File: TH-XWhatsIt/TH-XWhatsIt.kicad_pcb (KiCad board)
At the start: 2 copper layers, 175 x 128.1 mm, 36 parts, among them J1 MODEL F, J2 EXPANSION, J3 EXPANSION HEADER, J4 EXPANSION BEAMSPRING, J5 BEAMSPRING CONNECTOR, J6 EXPANSION BEAMSPRING, J7 EXPANSION DISPLAYWRITER, J8 DISPLAYWRITER CONNECTOR, J9 EXPANSION DISPLAYWRITER, SW1 SW_Push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

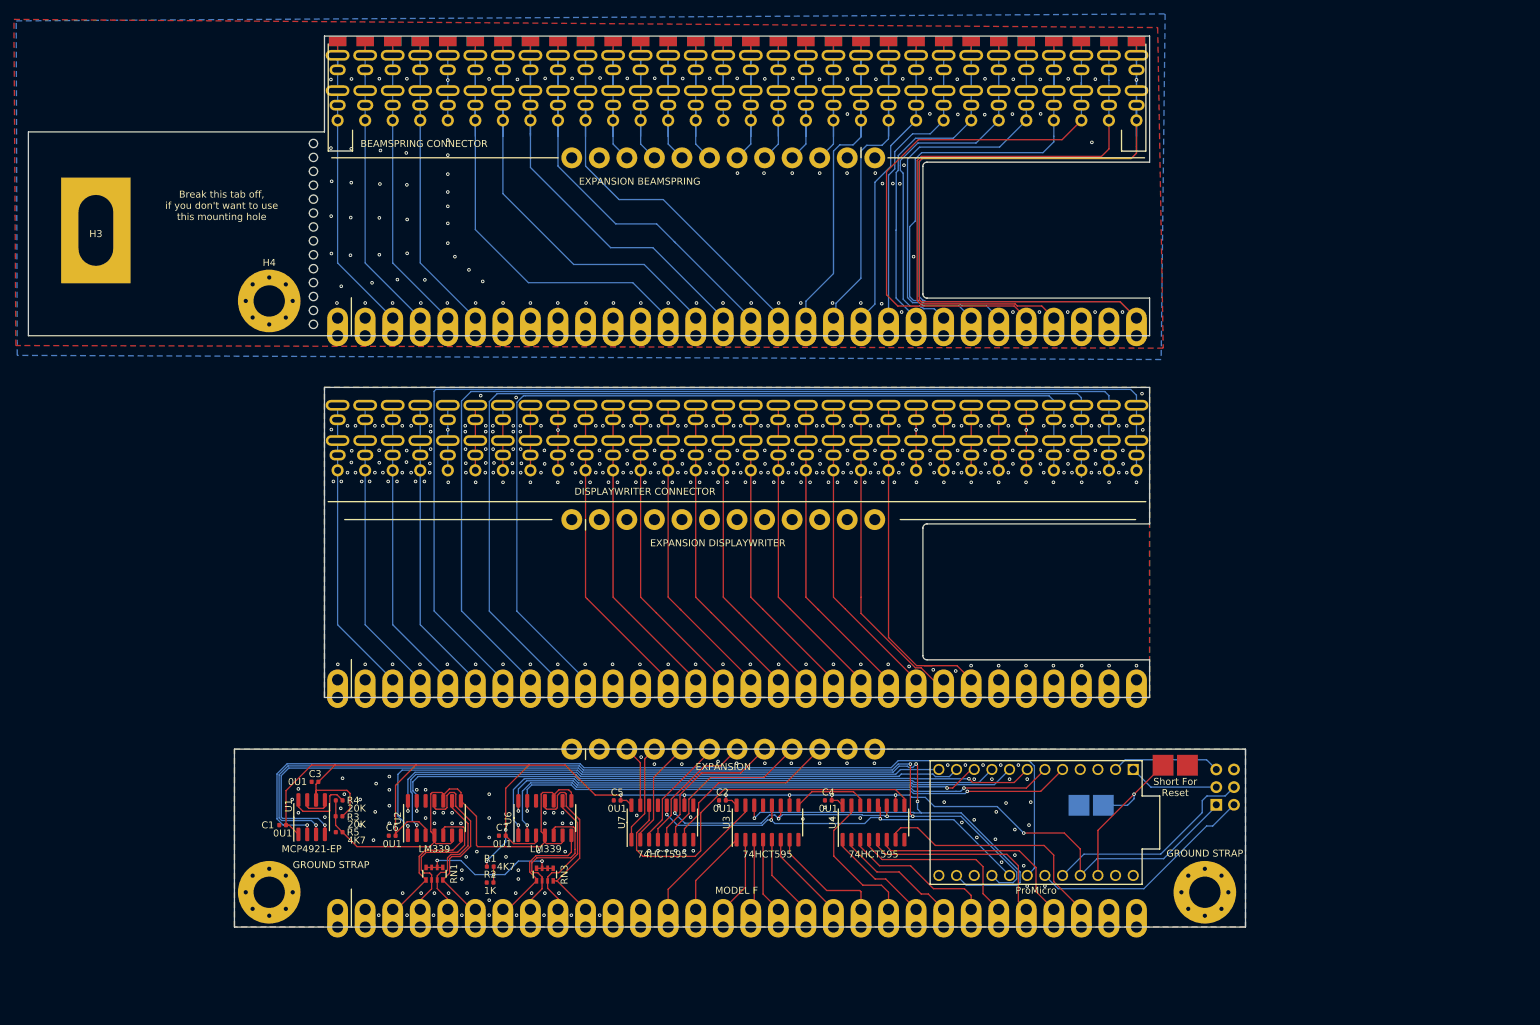
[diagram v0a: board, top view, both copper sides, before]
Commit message: Added compact beamspring-only version
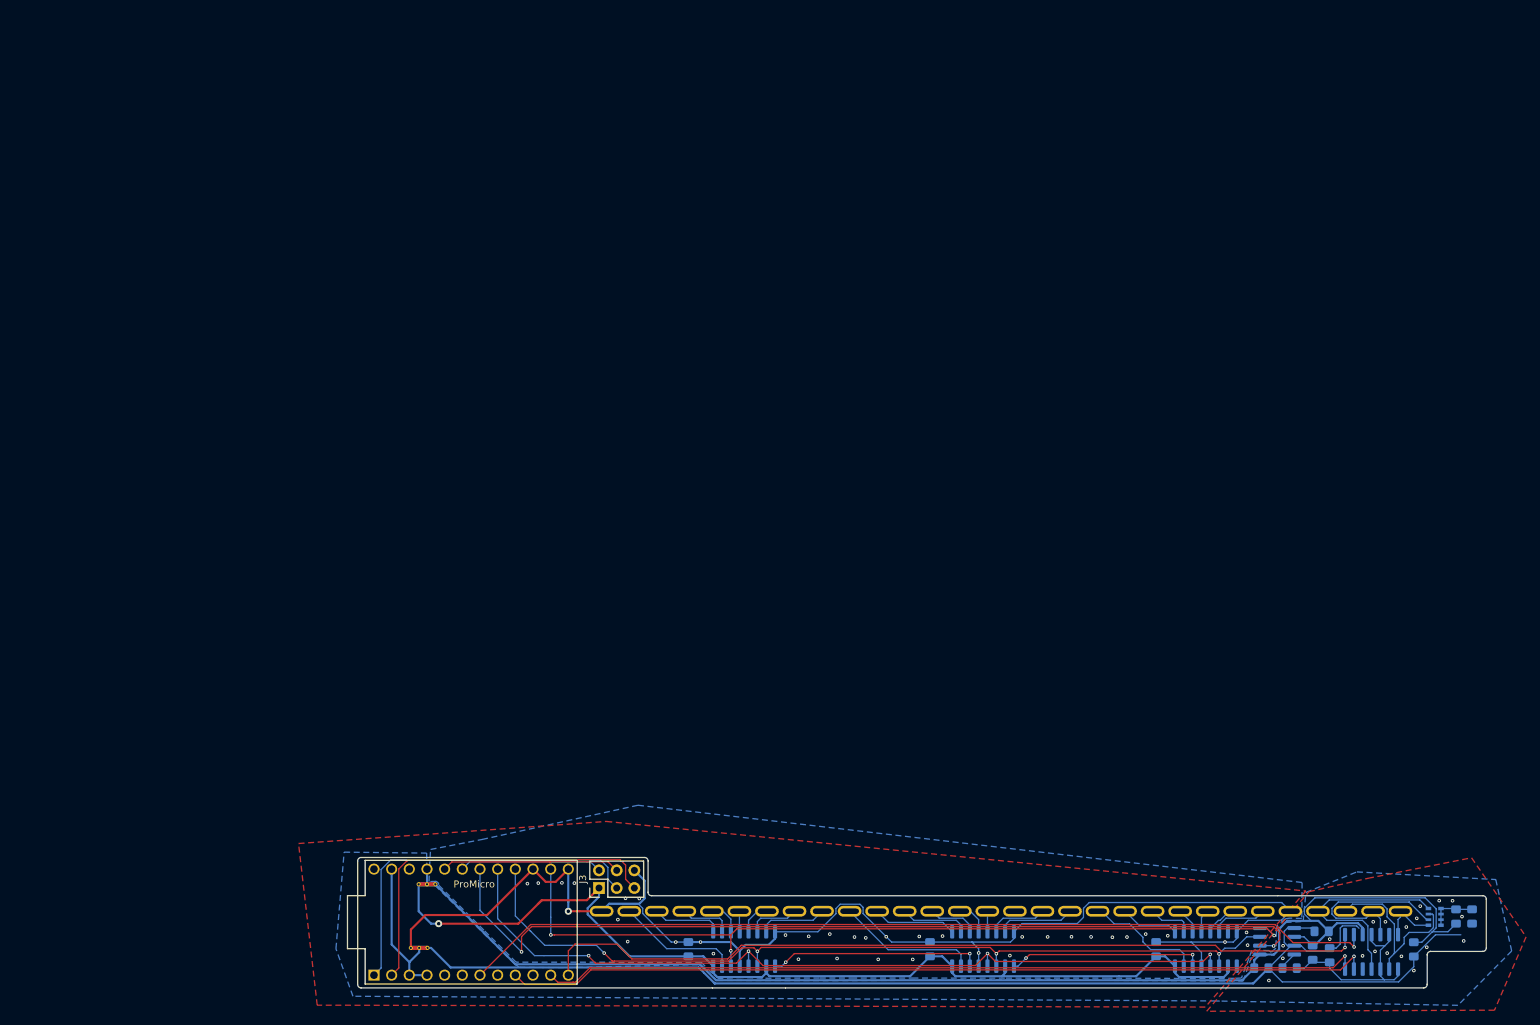
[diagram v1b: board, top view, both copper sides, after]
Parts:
- removed C7: 0U1, Capacitor_SMD:C_0402_1005Metric
- removed H1, H2: GROUND STRAP, MountingHole:MountingHole_4.5mm_Pad_Via
- removed H3: MountingHole_Pad, TH-XWhatsIt:BeamSpringGroundingMountingHole
- removed H4: MountingHole_Pad, MountingHole:MountingHole_4.5mm_Pad_Via
- removed J2: EXPANSION, TH-XWhatsIt:12-pin-castelated-connector
- removed J4: EXPANSION BEAMSPRING, TH-XWhatsIt:30-pin-castelated-connector
- removed J5: BEAMSPRING CONNECTOR, TH-XWhatsIt:30-pin-universal-beamspring-connector_v2
- removed J6: EXPANSION BEAMSPRING, TH-XWhatsIt:12-pin-castelated-connector
- removed J7: EXPANSION DISPLAYWRITER, TH-XWhatsIt:30-pin-castelated-connector
- removed J8: DISPLAYWRITER CONNECTOR, TH-XWhatsIt:30-pin-universal-displaywriter-connector_v2
- removed J9: EXPANSION DISPLAYWRITER, TH-XWhatsIt:12-pin-castelated-connector
- removed RN3: 100K, Resistor_SMD:R_Array_Convex_4x0603
- removed SW1, SW2: SW_Push, TH-XWhatsIt:PadsToShort
- removed U6: LM339, Package_SO:SOIC-14_3.9x8.7mm_P1.27mm
- added NT1: Net-Tie_3, NetTie:NetTie-3_THT_Pad0.3mm, B.Cu at (101.2, 155.0)
- added NT2: Net-Tie_3, NetTie:NetTie-3_THT_Pad0.3mm, B.Cu at (102.3, 145.9)
- C1, C2, C3, C4, C5, C6: footprint Capacitor_SMD:C_0402_1005Metric -> Capacitor_SMD:C_0805_2012Metric_Pad1.15x1.40mm_HandSolder; moved to B.Cu
- J1: value MODEL F -> BEAMSPRING CONNECTOR; footprint TH-XWhatsIt:30-pin-castelated-connector -> TH-XWhatsIt:30-pin-universal-beamspring-connector_v2
- J3: moved to F.Cu
- R1, R2, R3, R4, R5: footprint Resistor_SMD:R_0402_1005Metric -> Resistor_SMD:R_0805_2012Metric_Pad1.15x1.40mm_HandSolder; moved to B.Cu
- RN1, U1, U2, U3, U4, U7: moved to B.Cu
- moved C3 159.8 mm to (245.3, 155.2), turned to 90 degrees
- moved RN1 143.9 mm to (248.3, 150.5), turned to 180 degrees
- moved R5 143.5 mm to (233.2, 156.1), turned to 270 degrees
- moved C1 142.2 mm to (223.4, 157.9), turned to 180 degrees
- moved R3 141.3 mm to (230.8, 155.7), turned to 90 degrees
- moved R2 141.2 mm to (253.7, 150.5), turned to 90 degrees
- moved U1 139.9 mm to (225.7, 154.0), turned to 0 degrees
- moved R1 139.0 mm to (251.4, 150.5), turned to 90 degrees
- moved R4 138.7 mm to (227.5, 157.9), turned to 180 degrees
- moved U2 136.1 mm to (239.3, 155.6), turned to 270 degrees
- moved C6 134.3 mm to (232.1, 152.6)
- moved J3 89.5 mm to (128.2, 146.4), turned to 90 degrees
- moved U5 82.5 mm to (109.8, 151.3), turned to 0 degrees
- moved C5 80.4 mm to (208.3, 155.2), turned to 270 degrees
- moved U7 80.2 mm to (215.4, 155.2), turned to 270 degrees
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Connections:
- C2 pad 1: GNDA -> GNDD
- C2 pad 2: +5VA -> +5VD
- C4 pad 1: GNDA -> GNDD
- C4 pad 2: +5VA -> +5VD
- C5 pad 1: GNDA -> GNDD
- C5 pad 2: +5VA -> +5VD
- J1 pad 1: GNDA -> SENSE1
- J1 pad 10: SENSE8 -> COL19
- J1 pad 11: GNDA -> COL18
- J1 pad 12: GNDA -> COL17
- J1 pad 13: COL1 -> COL16
- J1 pad 14: COL2 -> COL15
- J1 pad 15: COL3 -> Net-(J1-Pad15)
- J1 pad 16: COL4 -> COL14
- J1 pad 17: COL5 -> COL13
- J1 pad 18: COL6 -> COL12
- J1 pad 19: COL7 -> COL11
- J1 pad 2: GNDA -> SENSE2
- J1 pad 20: COL8 -> COL10
- J1 pad 22: COL10 -> COL8
- J1 pad 23: COL11 -> COL7
- J1 pad 24: COL12 -> COL6
- J1 pad 25: COL13 -> COL5
- J1 pad 26: COL14 -> COL4
- J1 pad 27: COL15 -> COL3
- J1 pad 28: COL16 -> COL2
- J1 pad 29: GNDA -> COL1
- J1 pad 3: SENSE1 -> SENSE3
- J1 pad 30: GNDA -> GNDD
- J1 pad 4: SENSE2 -> SENSE4
- J1 pad 5: SENSE3 -> GNDD
- J1 pad 6: SENSE4 -> COL23
- J1 pad 7: SENSE5 -> COL22
- J1 pad 8: SENSE7 -> COL21
- J1 pad 9: SENSE6 -> COL20
- J3 pad 1: +5VA -> +5VD
- J3 pad 6: GNDA -> GNDD
- U3 pad 10: +5VA -> +5VD
- U3 pad 13: GNDA -> GNDD
- U3 pad 16: +5VA -> +5VD
- U3 pad 8: GNDA -> GNDD
- U4 pad 10: +5VA -> +5VD
- U4 pad 13: GNDA -> GNDD
- U4 pad 16: +5VA -> +5VD
- U4 pad 8: GNDA -> GNDD
- U5 pad 13: GNDA -> GNDD
- U5 pad 15: GNDA -> GNDD
- U5 pad 21: +5VA -> Net-(NT2-Pad2)
- U5 pad 23: GNDA -> Net-(NT1-Pad2)
- U5 pad 3: GNDA -> Net-(NT1-Pad2)
- U5 pad 4: GNDA -> Net-(NT1-Pad2)
- U7 pad 10: +5VA -> +5VD
- U7 pad 13: GNDA -> GNDD
- U7 pad 16: +5VA -> +5VD
- U7 pad 7: COL24 -> Net-(U7-Pad7)
- U7 pad 8: GNDA -> GNDD
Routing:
- net /beamspring plugboard/BSGROUND: track 217.0 -> 0.00 mm, vias 103 -> 0
- net GNDD: track 0.00 -> 198.9 mm, vias 0 -> 37
- net GNDA: track 4.68 -> 182.5 mm, vias 109 -> 19
- net /displaywriter plugboard/DWSENSE5: track 158.6 -> 0.00 mm
- net /displaywriter plugboard/DWSENSE6: track 149.4 -> 0.00 mm
- net +5VD: track 0.00 -> 144.4 mm, vias 0 -> 1
- net /displaywriter plugboard/DWSENSE7: track 141.9 -> 0.00 mm
- net /displaywriter plugboard/DWSENSE8: track 132.0 -> 0.00 mm
- net /beamspring plugboard/BSCOL15: track 86.6 -> 0.00 mm
- net /beamspring plugboard/BSCOL14: track 84.8 -> 0.00 mm
- net ROW7: track 84.1 -> 0.00 mm, vias 2 -> 0
- net ROW8: track 83.7 -> 0.00 mm, vias 2 -> 0
- net ROW5: track 80.2 -> 0.00 mm, vias 1 -> 0
- net /beamspring plugboard/BSCOL13: track 76.5 -> 0.00 mm
- net /beamspring plugboard/BSCOL1: track 75.2 -> 0.00 mm
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- added copper zone on B.Cu, net GNDD
- added copper zone on F.Cu, net GNDD
- removed copper zone on B.Cu, net /beamspring plugboard/BSGROUND
- removed copper zone on F.Cu, net /beamspring plugboard/BSGROUND
- removed copper zone on B.Cu, net /displaywriter plugboard/DWGROUND
- removed copper zone on F.Cu, net /displaywriter plugboard/DWGROUND
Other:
- board size 175 x 128.1 mm -> 162.2 x 18.8 mm
- net class Power added: clearance 0.1524, trace_width 0.3048, via_dia 0.508, via_drill 0.254
- board text removed: "Break this tab off, if you don't want to use this mounting hole"
- board text removed: "Short For Reset"

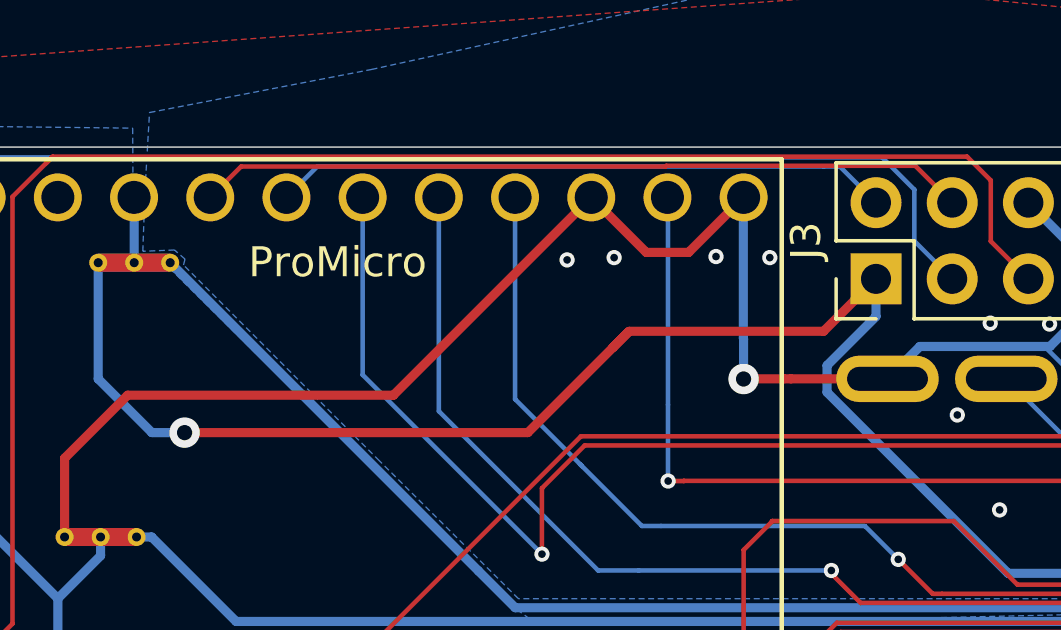
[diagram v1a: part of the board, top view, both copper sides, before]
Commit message: added version selection resistor divider pads
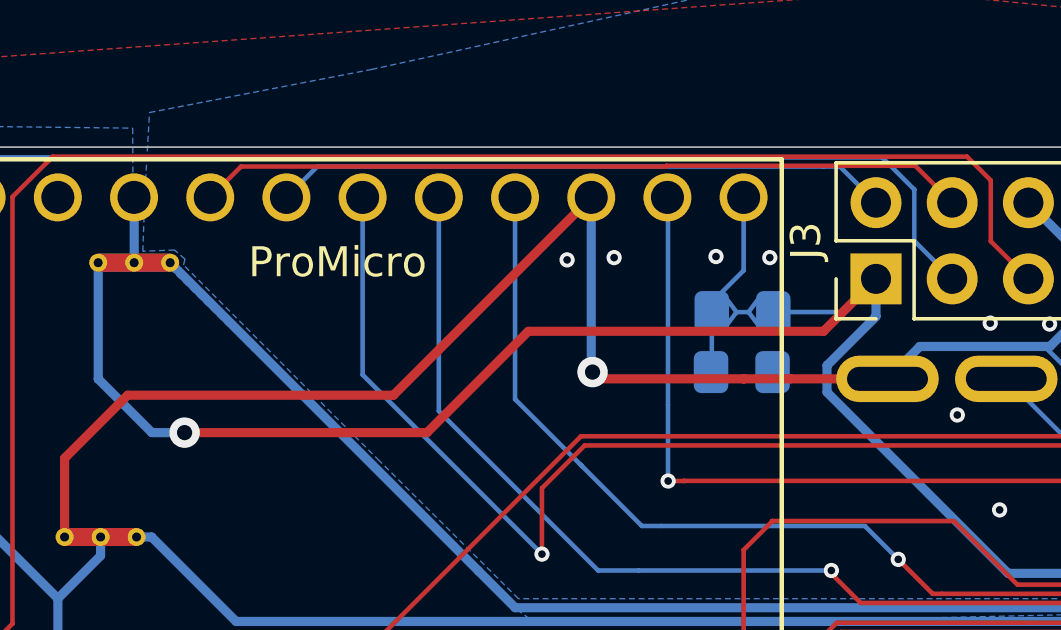
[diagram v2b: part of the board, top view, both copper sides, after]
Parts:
- added R6: Not Mounted, Shorted, TH-XWhatsIt:SHORTEDR_0805_2012Metric_Pad1.15x1.40mm_HandSolder, B.Cu at (123.8, 147.5)
- added R7: Not Mounted, Resistor_SMD:R_0805_2012Metric_Pad1.15x1.40mm_HandSolder, B.Cu at (123.7, 149.5)
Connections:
- U5 pad 13: GNDD -> Net-(R6-Pad2)
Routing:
- net Net-(R6-Pad2): track 0.00 -> 6.30 mm
- net +5VD: track 144.4 -> 147.6 mm
- net GNDD: track 198.9 -> 197.2 mm

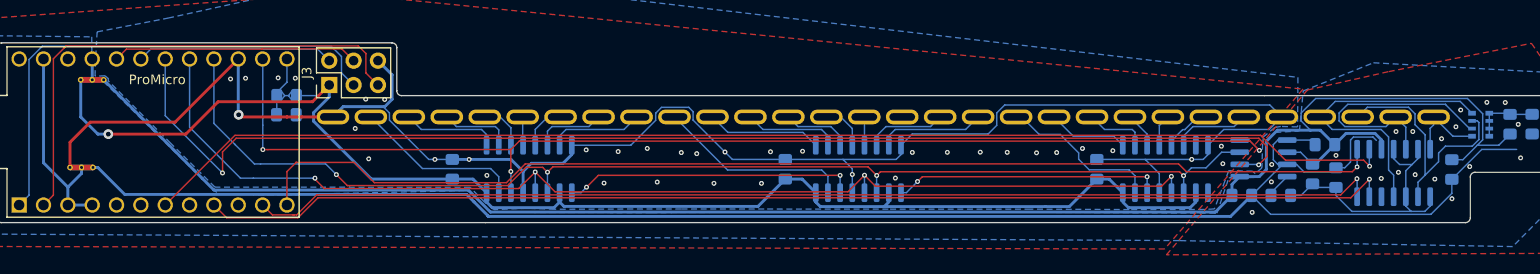
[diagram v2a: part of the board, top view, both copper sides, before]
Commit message: cleaned away some extra copper traces around pads connected to copper fills
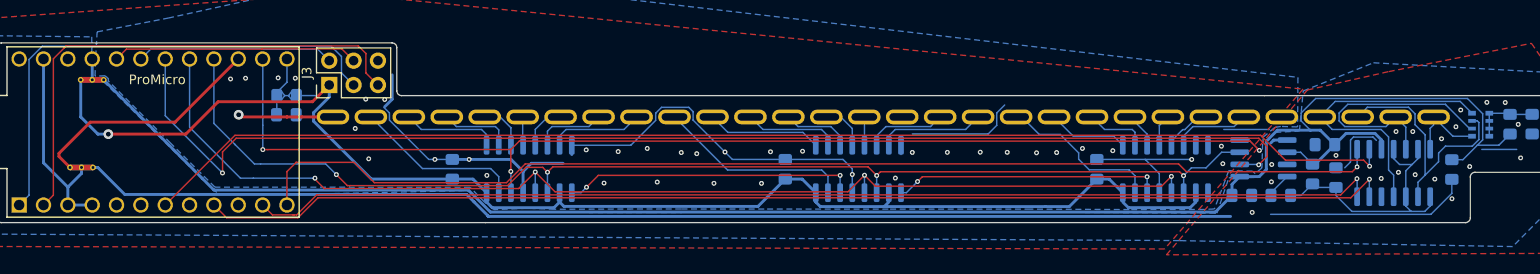
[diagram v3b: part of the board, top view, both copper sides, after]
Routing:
- net GNDD: track 197.2 -> 134.0 mm
- net GNDA: track 182.5 -> 156.2 mm
